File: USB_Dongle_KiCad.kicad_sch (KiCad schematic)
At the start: 56 parts, among them J1 USB_C_Receptacle_USB2.0, J2 Conn SWD 02x05, J3 DM3BT-DSF-PEJS, SW1 PCM12SMTR, SW2 KMR223G LFG, U1 AMS1117-3.3, U2 STULPI01A, U3 USBULC6-2M6, U4 ESDA14V2-2BF3, U5 STM32F730R8Tx, U6 CAT811TTBI-GT3, Y1 3225 SMD Oscillator, Y2 24MHz / 10pF / 20ppm

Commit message: Update: New routing after ULPI component change
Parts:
- removed C5: 100n, Capacitor_SMD:C_0603_1608Metric, symbol Device:C_Small
- removed U2: STULPI01A, Package_BGA:ST_uTFBGA-36_3.6x3.6mm_Layout6x6_P0.5mm, symbol Interface_USB:STULPI01A
- added C8: 1u, Capacitor_SMD:C_0805_2012Metric, symbol Device:C_Small
- added R6: 22R, Resistor_SMD:R_0603_1608Metric, symbol Device:R_Small_US
- added U2: USB3343, Package_DFN_QFN:QFN-24-1EP_4x4mm_P0.5mm_EP2.6x2.6mm, symbol Interface_USB:USB3343
- C7: value 1.5u -> 1u
- C9: value 1.5u -> 100n
- R1: value 2.2k -> 20k
- R2: value 12k -> 8.06k
- Y1: value 3225 SMD Oscillator -> 26 MHz
- renumbered C28 to C25, C25 to C26, C26 to C27, C27 to C28, C6 to C5, C8 to C6, R11 to R10, R9 to R11, R10 to R12, R6 to R7, R7 to R8, R8 to R9
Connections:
- net +3.3V: now also C4.2, C9.1, U2.16 (VBAT), U2.9 (VDDIO); no longer C4.1
- net GND: now also C4.1, C8.2, U2.25 (GND); no longer C4.2
- net ULPI_CLK: now also R6.2
- net ULPI_D0: now also U2.4 (DATA0)
- net ULPI_D1: now also U2.5 (DATA1)
- net ULPI_D2: now also U2.6 (DATA2)
- net ULPI_D3: now also U2.7 (DATA3)
- net ULPI_D4: now also U2.8 (DATA4)
- net ULPI_D5: now also U2.10 (DATA5)
- net ULPI_D6: now also U2.11 (DATA6)
- net ULPI_D7: now also U2.12 (DATA7)
- net ULPI_DIR: now also U2.1 (DIR)
- net ULPI_NXT: now also U2.3 (NXT)
- net ULPI_RESET: now also U2.22 (~{RESETB})
- net ULPI_STP: now also U2.24 (STP)
- net USB_D+: now also U2.13 (DP)
- net USB_D-: now also U2.14 (DM)
- net at Y1.3: now also U2.21 (REFCLK/XI)
- net at C7.1: now also U2.15 (VDD33), U2.18 (ID)
- net at R1.2: now also U2.17 (VBUS)
- net at R2.2: now also U2.19 (RBIAS)
- new net: R6.1, U2.2 (CLKOUT)
- new net: C8.1, U2.23 (VDD18)
- no-connect marks 31 -> 29
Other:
- note added: "<1 ohm ESR"
- note added: "SMD Clock oscillator"
- note removed: "KC3225K20.0000C1GE00"
- moved on the sheet: C2, R1

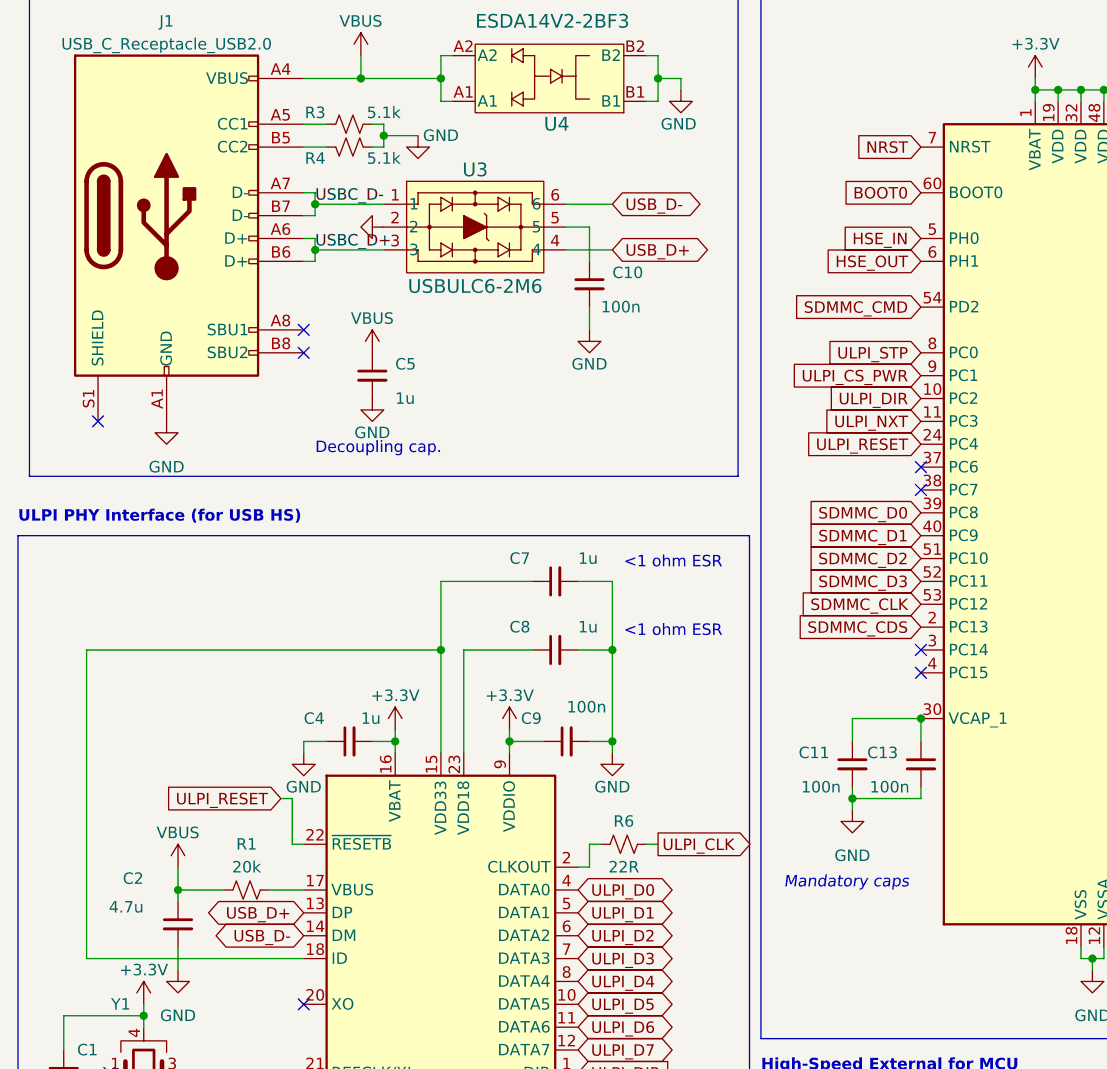
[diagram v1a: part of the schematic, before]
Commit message: Fix: Value of external capacitor for VCAP1
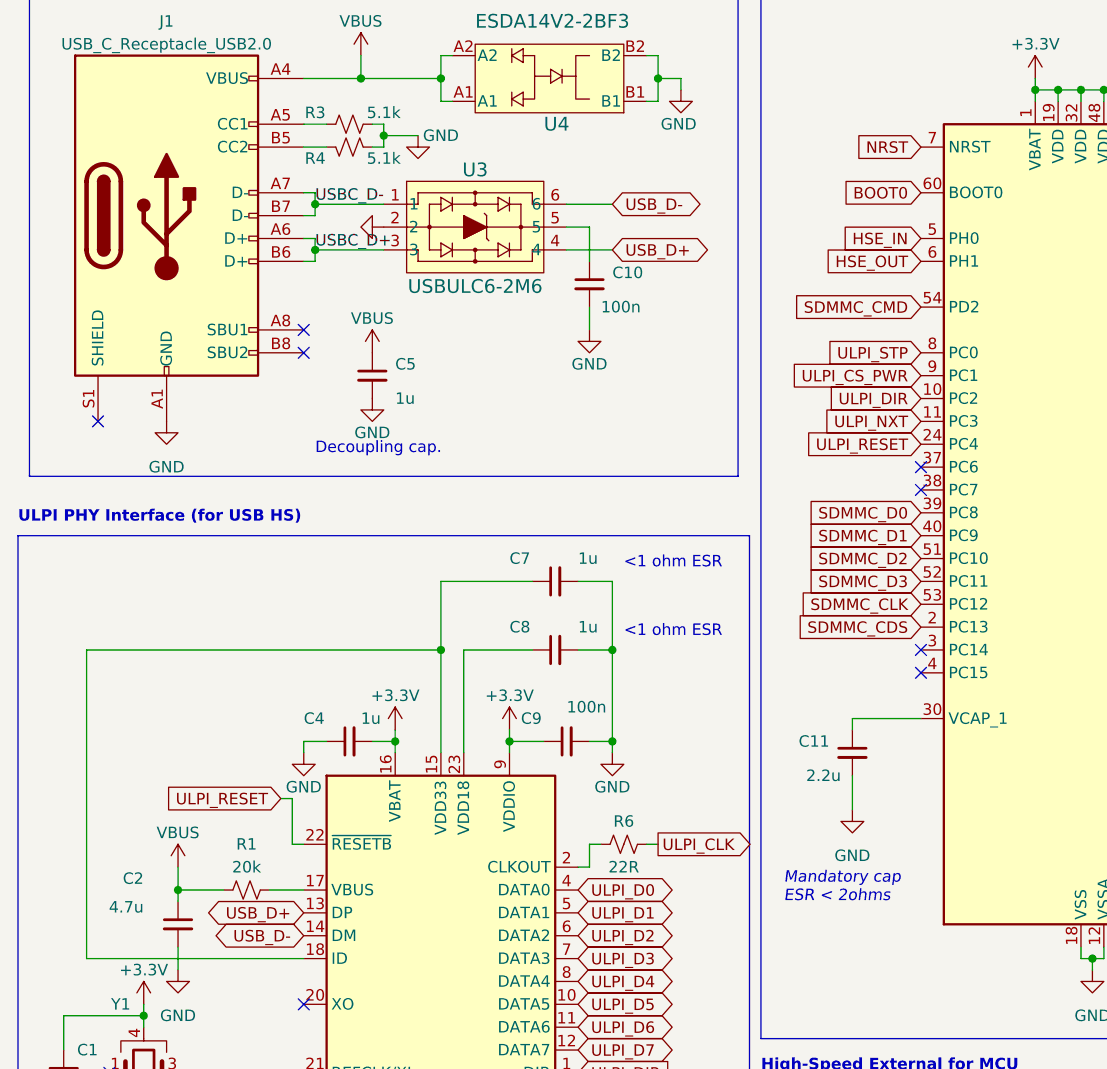
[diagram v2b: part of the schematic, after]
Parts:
- removed C13: 100n, Capacitor_SMD:C_0603_1608Metric, symbol Device:C_Small
- C11: value 100n -> 2.2u
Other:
- note added: "Mandatory cap ESR < 2ohms"
- note removed: "Mandatory caps"
- moved on the sheet: C11
